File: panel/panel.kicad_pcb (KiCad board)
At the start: 2 copper layers, 80.9 x 128.5 mm, 4 parts

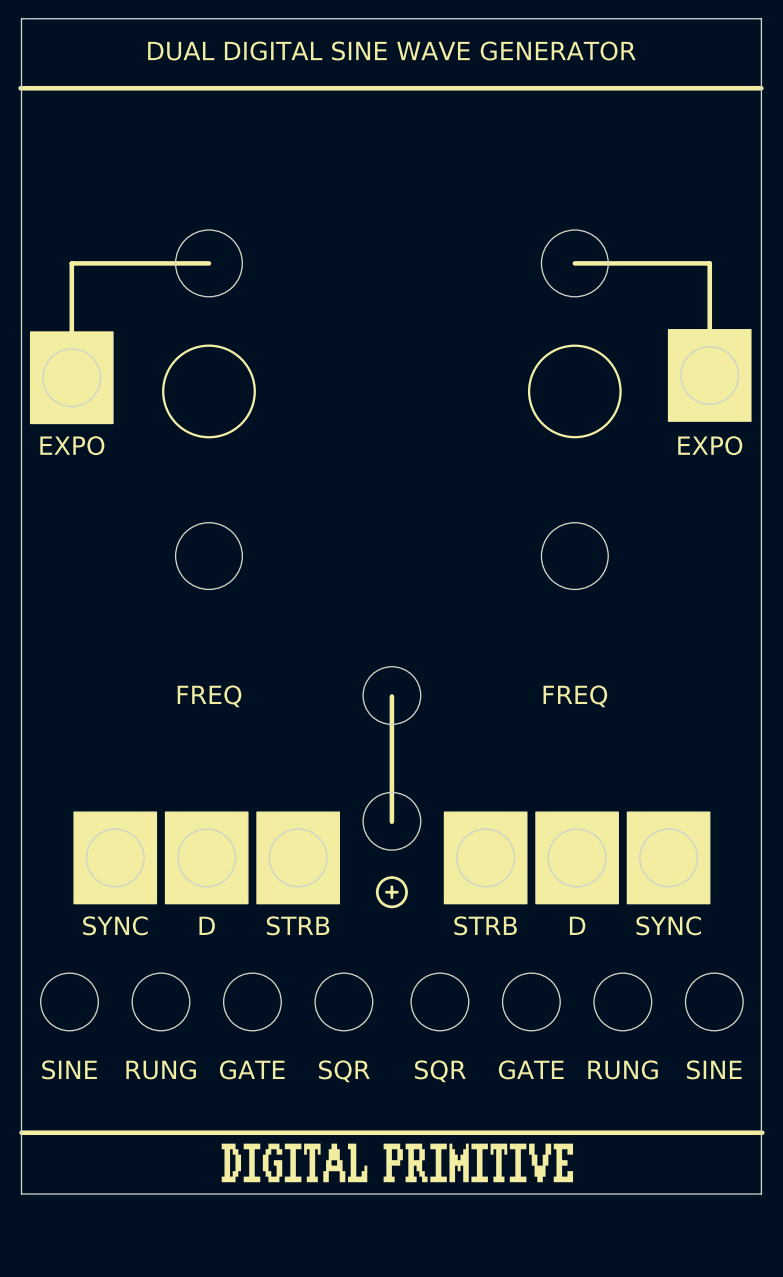
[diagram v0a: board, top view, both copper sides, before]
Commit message: Rejigged layout for more space
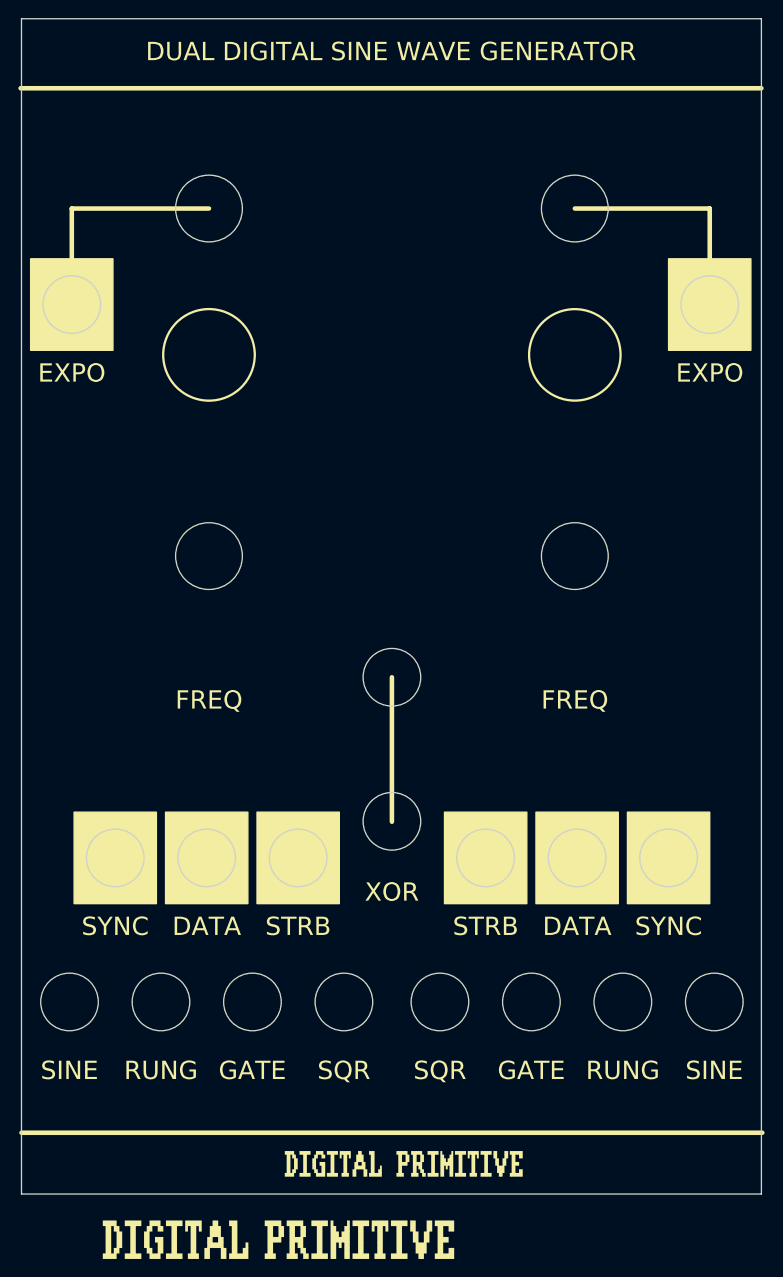
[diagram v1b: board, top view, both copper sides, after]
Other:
- outline, holes or cut-outs redrawn
- board text added: "DATA"
- board text added: "XOR"
- board text removed: "D"

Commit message: Removed the unneccessary 100ohm resistor after the expo converter
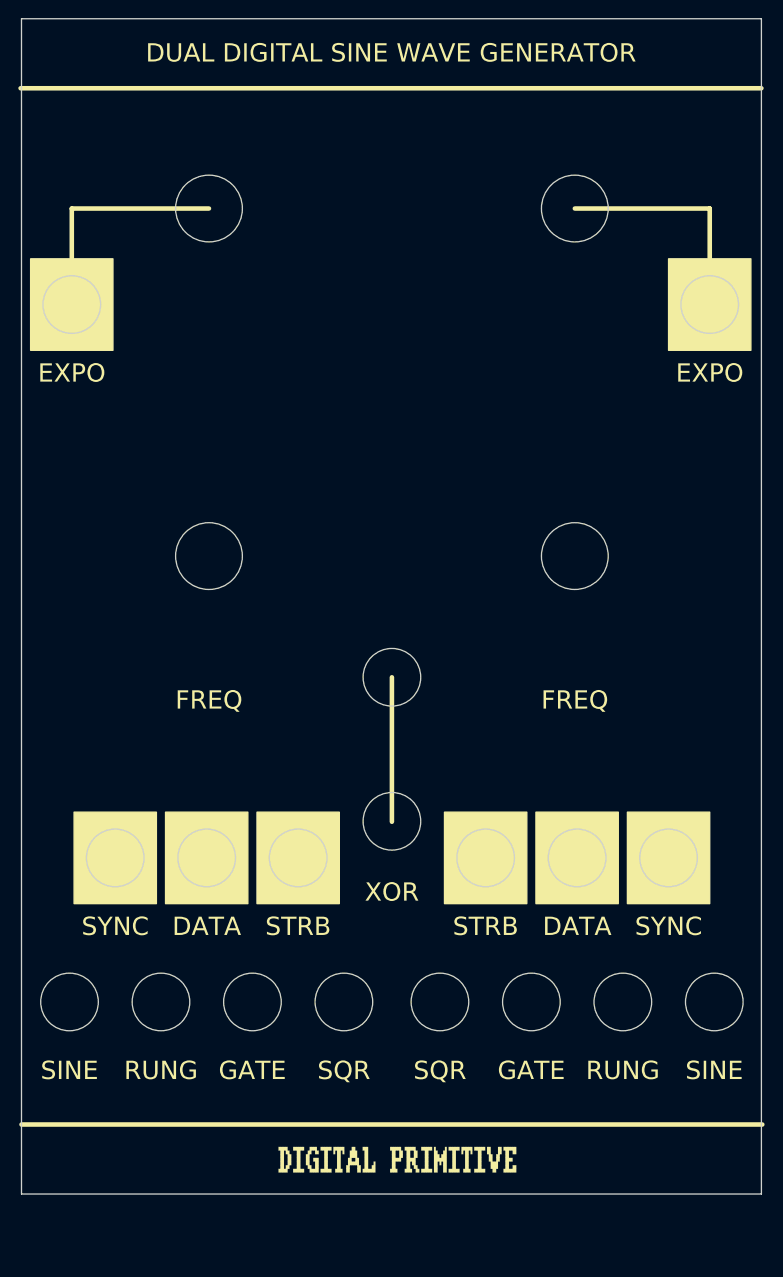
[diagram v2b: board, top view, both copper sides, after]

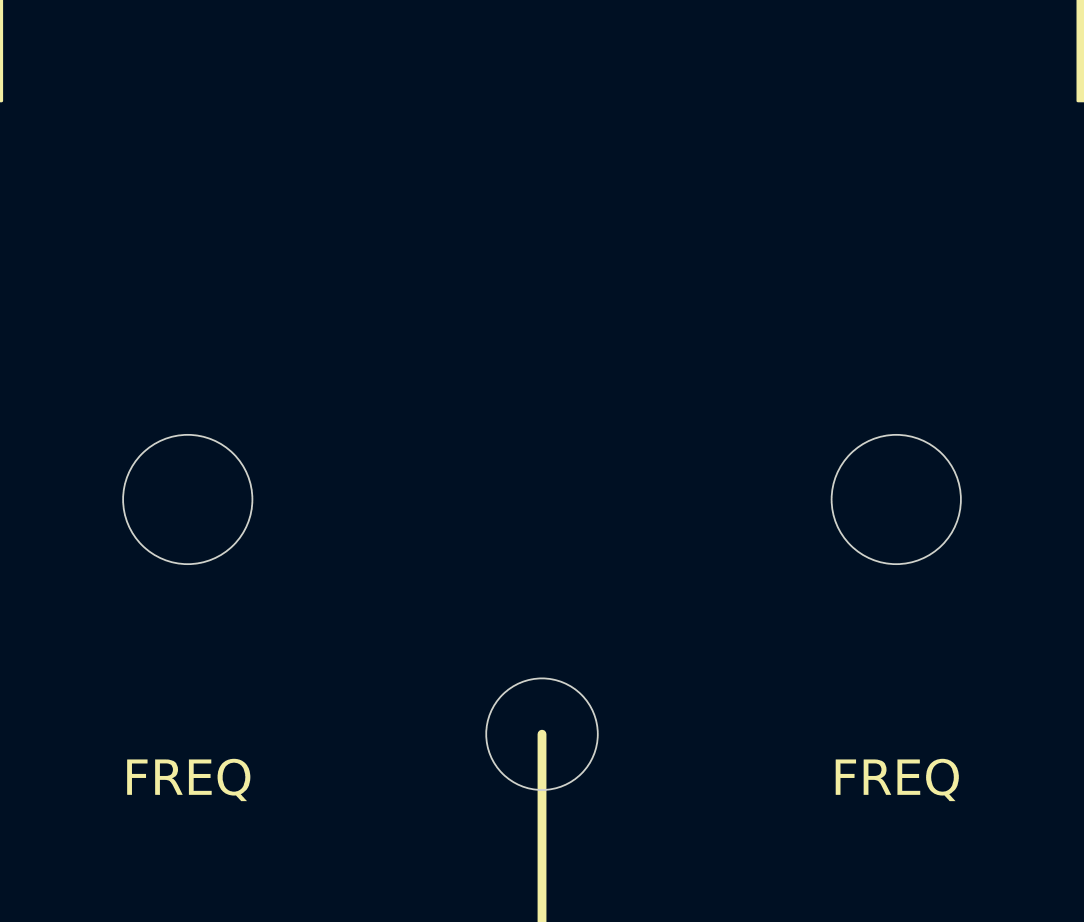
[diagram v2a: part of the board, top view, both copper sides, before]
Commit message: Added range switch
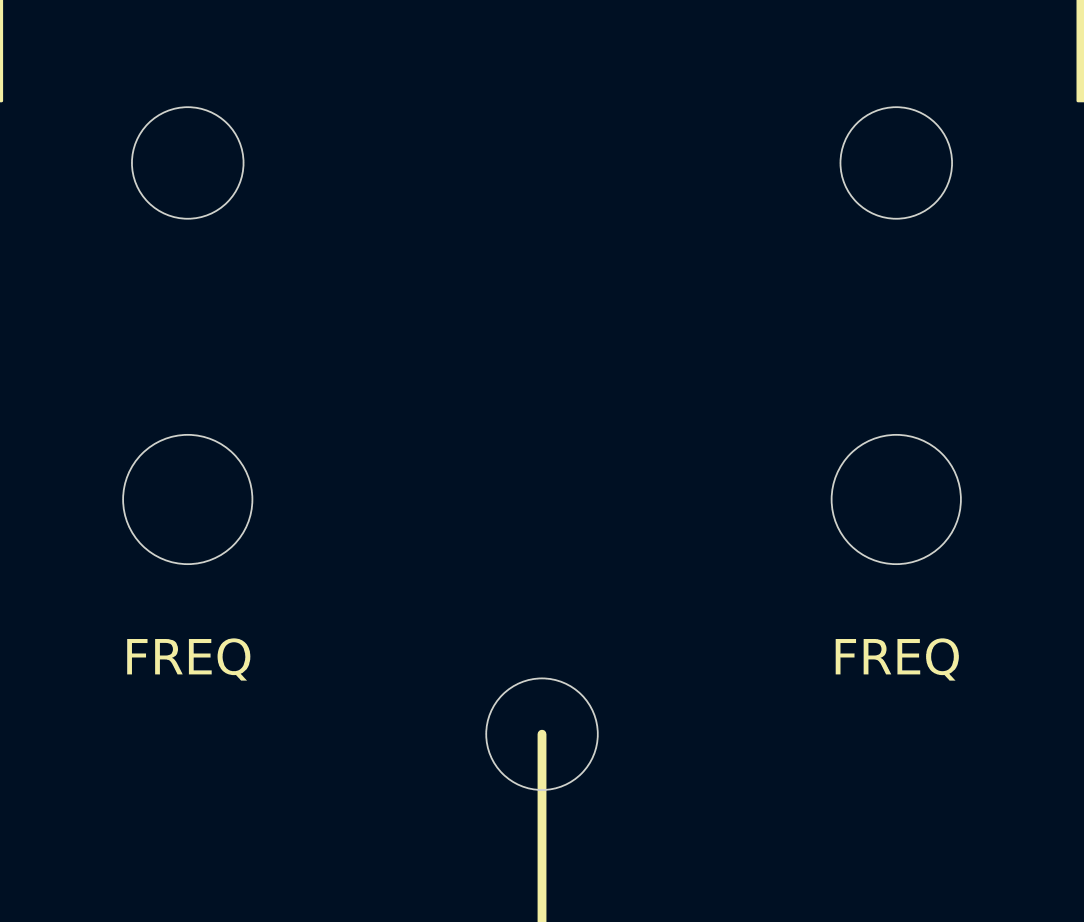
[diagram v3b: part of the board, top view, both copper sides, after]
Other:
- outline, holes or cut-outs redrawn
